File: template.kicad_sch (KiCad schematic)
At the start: 1 part

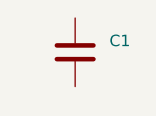
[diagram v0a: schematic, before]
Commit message: added rules
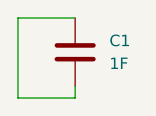
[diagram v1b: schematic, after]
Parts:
- C1: value (none) -> 1F; footprint (none) -> Capacitor_SMD:C_0805_2012Metric
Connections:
- net at C1.1: now also C1.2
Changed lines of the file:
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@@
     (company "E-Agle TRT")
+  )
+  (wire (pts (xy 199.39 121.92) (xy 193.04 121.92))
+    (stroke (width 0) (type default) (color 0 0 0 0))
+  )
+  (wire (pts (xy 193.04 121.92) (xy 193.04 130.81))
+    (stroke (width 0) (type default) (color 0 0 0 0))
+  )
+  (wire (pts (xy 199.39 130.81) (xy 199.39 129.54))
+    (stroke (width 0) (type default) (color 0 0 0 0))
+  )
+  (wire (pts (xy 193.04 130.81) (xy 199.39 130.81))
+    (stroke (width 0) (type default) (color 0 0 0 0))
   )
   (symbol (lib_id "Device:C") (at 199.39 125.73 0) (unit 1)
@@
       (effects (font (size 1.27 1.27)) (justify left))
     )
-    (property "Value" "" (id 1) (at 203.2 126.9999 0)
+    (property "Value" "1F" (id 1) (at 203.2 126.9999 0)
       (effects (font (size 1.27 1.27)) (justify left))
     )
-    (property "Footprint" "" (id 2) (at 200.3552 129.54 0)
+    (property "Footprint" "Capacitor_SMD:C_0805_2012Metric" (id 2) (at 200.3552 129.54 0)
       (effects (font (size 1.27 1.27)) hide)
     )
